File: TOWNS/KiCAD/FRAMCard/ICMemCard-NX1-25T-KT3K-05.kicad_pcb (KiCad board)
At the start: 2 copper layers, 79.1 x 50.5 mm, 19 parts, among them J1 PCMCIA_Connector, Q1 BC846X, Q2 BC846X, U1 FM18W08-SGTR, U2 FM18W08-SGTR, U3 74AHCT1G32

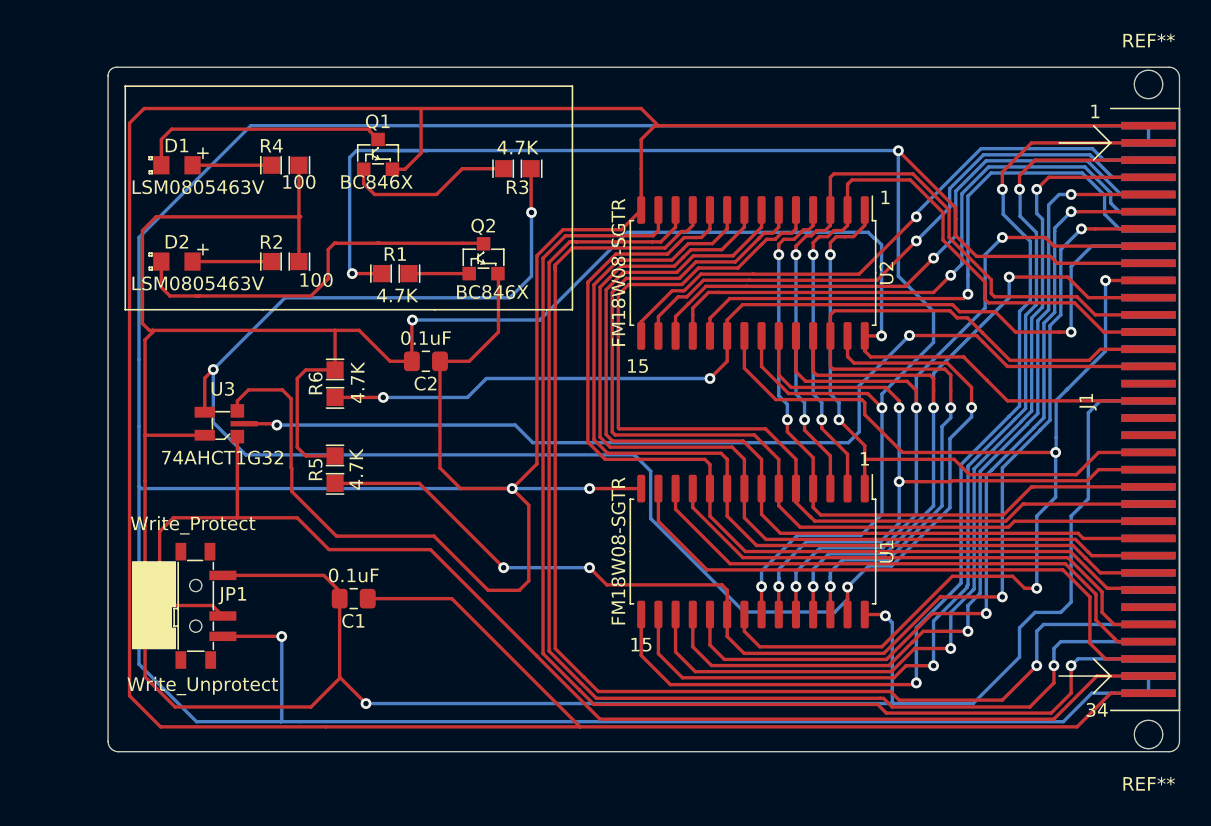
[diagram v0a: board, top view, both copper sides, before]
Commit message: Working on PCBfor Hirose NX1 PCMCIA Frame
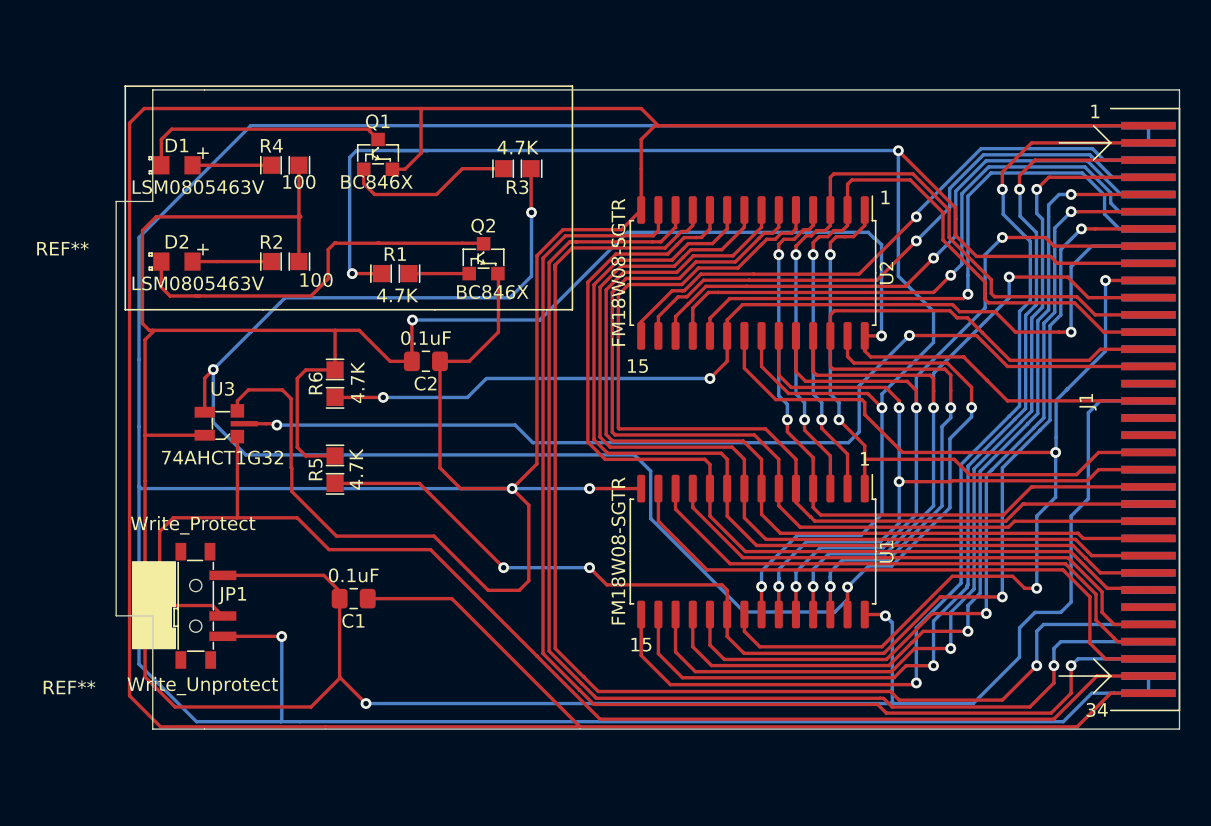
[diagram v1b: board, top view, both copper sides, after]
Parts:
- removed the REF** at (139.1, 99.9)
- removed the REF** at (139.1, 51.9)
- added REF**: MountingHole_1.5mm, MountingHole:MountingHole_2.1mm, F.Cu at (58.9, 60.4)
- added REF**: MountingHole_1.5mm, MountingHole:MountingHole_2.1mm, F.Cu at (59.3, 92.8)
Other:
- board size 79.1 x 50.5 mm -> 78.5 x 47.2 mm
- board text added: "FM TOWNS RESCUE BOOT MEMORY CARD Using HIROSE NX1 PCMCIA FRAME by Captain YS http://www.ysflight.com Ver. 20220514"
- board text added: "PCMCIA Connector"
- board text removed: "FM TOWNS RESCUE BOOT MEMORY CARD by Captain YS http://www.ysflight.com Ver. 20220514"
- board text removed: "PCMCIA Connector 95622-003LF"

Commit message: Added fillet
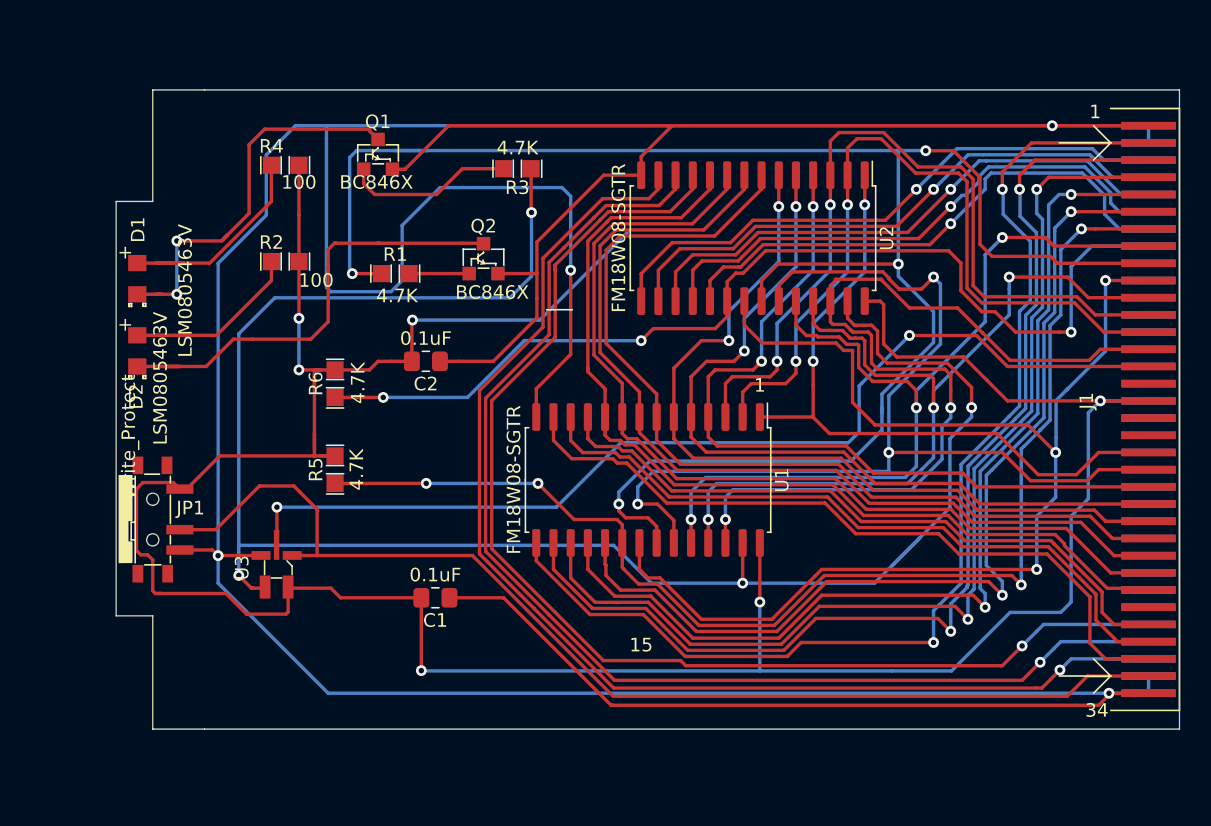
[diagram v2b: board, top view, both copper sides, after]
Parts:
- moved U3 11.3 mm to (74.7, 87.6), turned to 270 degrees
- moved REF** 9.67 mm to (68.5, 59.3)
- moved U1 9.38 mm to (102.1, 81.2)
- moved REF** 9.12 mm to (68.5, 92.5)
- moved D1 8.87 mm to (64.4, 66.3), turned to 90 degrees
- moved D2 7.22 mm to (64.4, 71.6), turned to 90 degrees
- moved JP1 7.12 mm to (65.5, 84.1)
- moved C1 6.03 mm to (86.4, 89.9)
- moved U2 2.57 mm to (109.9, 63.3)
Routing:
- net GND: track 555.9 -> 377.2 mm, vias 3 -> 4
- net Vcc: track 282.4 -> 212.6 mm, vias 4 -> 6
- net /A12: track 54.1 -> 75.6 mm
- net /Wp: track 96.8 -> 84.0 mm
- net /A6: track 70.7 -> 59.7 mm, vias 0 -> 2
- net Net-(D1-Pad1): track 18.6 -> 29.5 mm, vias 0 -> 2
- net Net-(D1-Pad2): track 5.83 -> 16.6 mm
- net /D0: track 39.5 -> 49.6 mm
- net /D1: track 41.6 -> 51.7 mm
- net /D7: track 62.5 -> 72.5 mm
- net /A11: track 82.5 -> 92.0 mm
- net /D2: track 44.8 -> 54.4 mm
- net /A5: track 70.6 -> 61.4 mm, vias 0 -> 2
- net /~OE: track 132.8 -> 141.9 mm
- net /D6: track 66.0 -> 74.7 mm
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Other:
- board text added: "Mounting Hole 2.1mm X 4.1mm Oval"
- board text removed: "Write_Unprotect"

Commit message: Cleaning up PCB
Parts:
- JP1: value Write_Protect -> WP
- U3: value 74AHCT1G32 -> SN74LS32DR; footprint PCMCIA:SOT353_Easy -> Package_SO:SOIC-14_3.9x8.7mm_P1.27mm
- moved U3 8.20 mm to (82.9, 88.1)
- moved C1 4.70 mm to (89.3, 93.5)
- moved R5 2.67 mm to (74.4, 80.4)
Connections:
- R1 pad 2: /~OE -> Net-(R1-Pad2)
- R3 pad 2: /~WE~orWP -> Net-(R3-Pad2)
- U3 pad 1: /Wp -> /WPorWP
- U3 pad 3: GND -> /~WE~orWP
- U3 pad 4: /~WE~orWP -> /Wp
- U3 pad 5: Vcc -> /Wp
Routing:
- net /~WE~orWP: track 136.5 -> 87.2 mm, vias 4 -> 3
- net /~OE: track 141.9 -> 103.5 mm, vias 4 -> 5
- net Net-(R3-Pad2): track 0.00 -> 38.3 mm, vias 0 -> 2
- net GND: track 377.2 -> 347.4 mm
- net Net-(R1-Pad2): track 0.00 -> 26.0 mm, vias 0 -> 2
- net /~WE: track 75.6 -> 64.3 mm
- net /WPorWP: track 0.00 -> 9.54 mm
- net /~CE1: track 91.8 -> 99.6 mm
- net Vcc: track 212.6 -> 204.8 mm
- net /Wp: track 84.0 -> 87.1 mm
- net /A14: track 68.0 -> 65.4 mm
- net /D11: track 43.7 -> 45.7 mm
- net /D7: track 72.5 -> 74.4 mm
- net /D12: track 42.7 -> 44.6 mm
- net /D6: track 74.7 -> 76.5 mm
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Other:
- outline, holes or cut-outs redrawn
- board text added: "FM TOWNS RESCUE BOOT MEMORY CARD Using HIROSE NX1 PCMCIA FRAME by Captain YS http://www.ysflight.com Ver. 20220520"
- board text removed: "FM TOWNS RESCUE BOOT MEMORY CARD Using HIROSE NX1 PCMCIA FRAME by Captain YS http://www.ysflight.com Ver. 20220514"

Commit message: Moving files around.
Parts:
- moved R5 32.8 mm to (106.2, 88.3), turned to 0 degrees
- moved R6 26.6 mm to (103.7, 73.3), turned to 180 degrees
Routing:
- net /~CE2: track 75.1 -> 48.3 mm, vias 3 -> 1
- net /~CE1: track 99.6 -> 75.2 mm
- net Vcc: track 204.8 -> 210.1 mm, vias 6 -> 7
- net /~OE: track 103.5 -> 104.6 mm
- net /A4: track 69.3 -> 70.0 mm
- net /A9: track 61.9 -> 62.4 mm

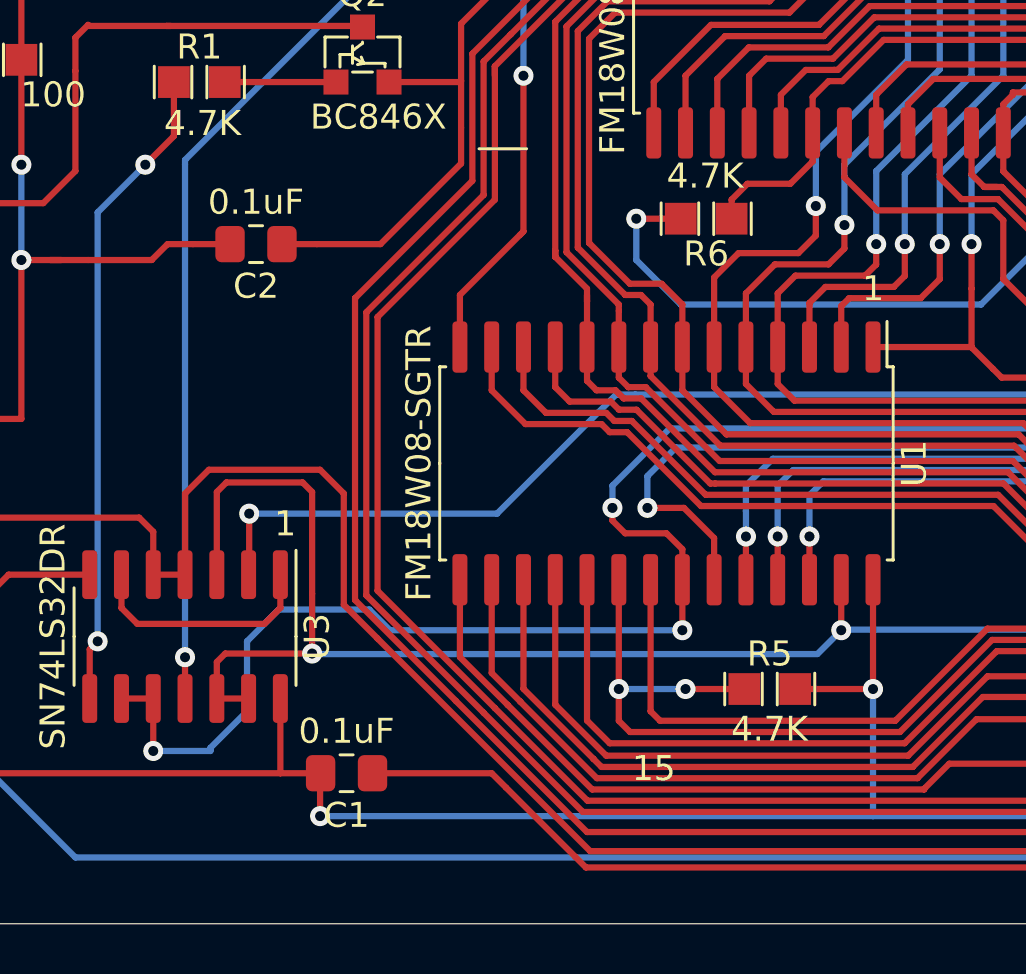
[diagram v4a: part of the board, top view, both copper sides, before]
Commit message: Better spacing between parts.
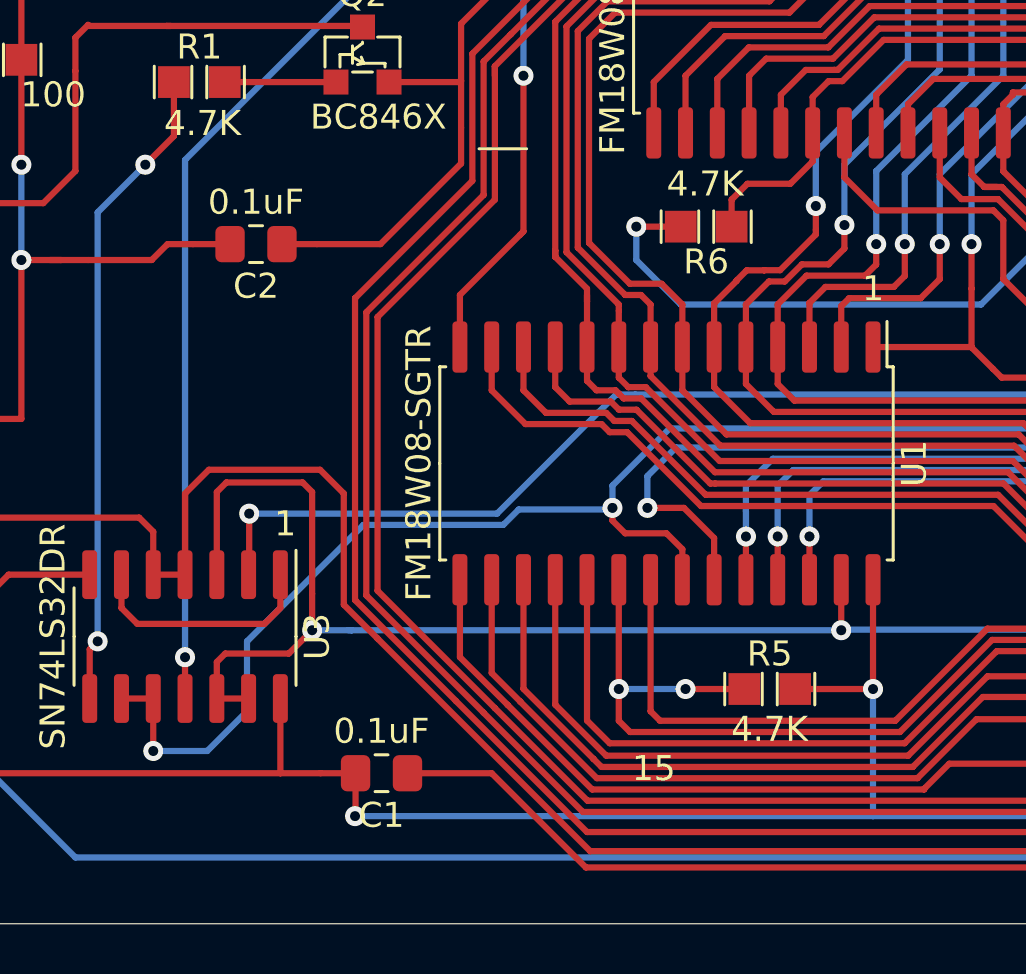
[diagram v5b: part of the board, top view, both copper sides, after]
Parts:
- moved C1 1.40 mm to (90.7, 93.5)
- moved R6 0.32 mm to (103.7, 73.6)
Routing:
- net /~OE: track 104.6 -> 101.0 mm, vias 5 -> 4
- net GND: track 347.4 -> 346.0 mm
- net /~WE~orWP: track 86.7 -> 85.9 mm
- net /A5: track 61.6 -> 61.0 mm

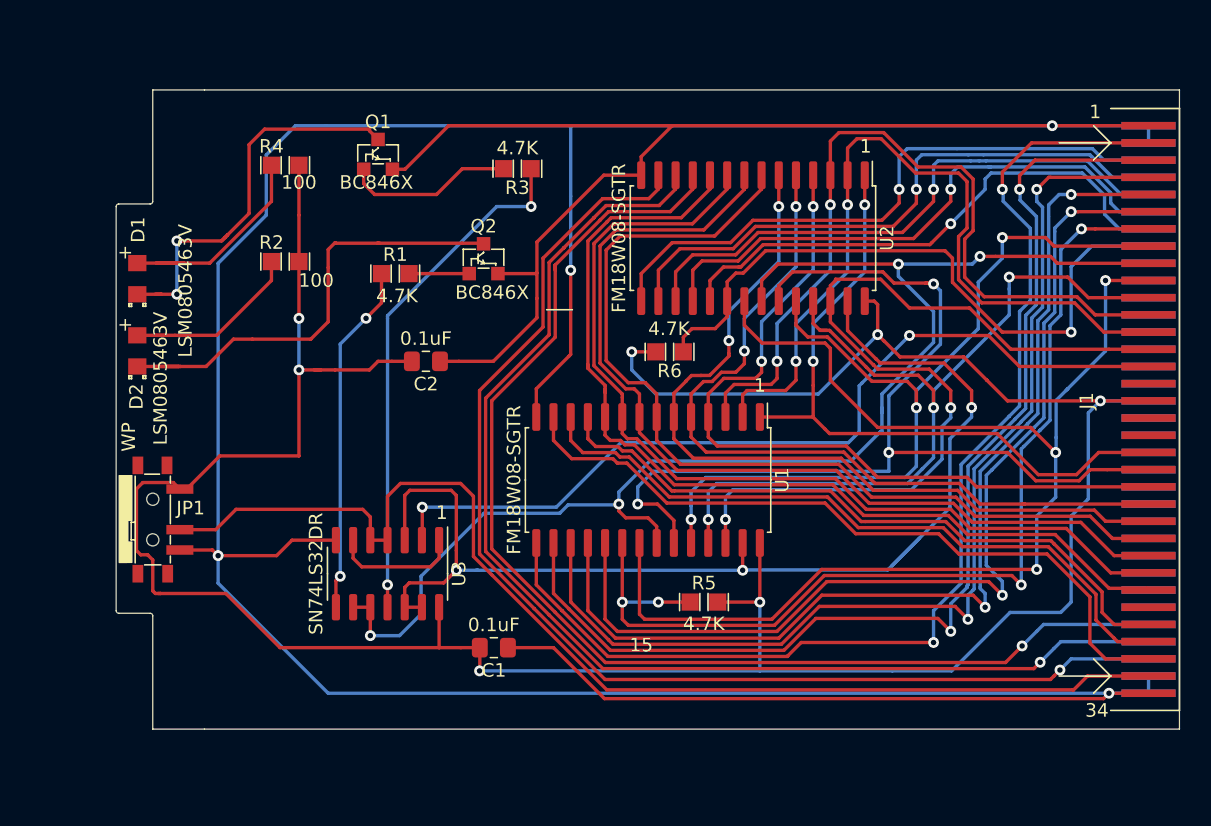
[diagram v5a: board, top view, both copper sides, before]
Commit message: Moving files around
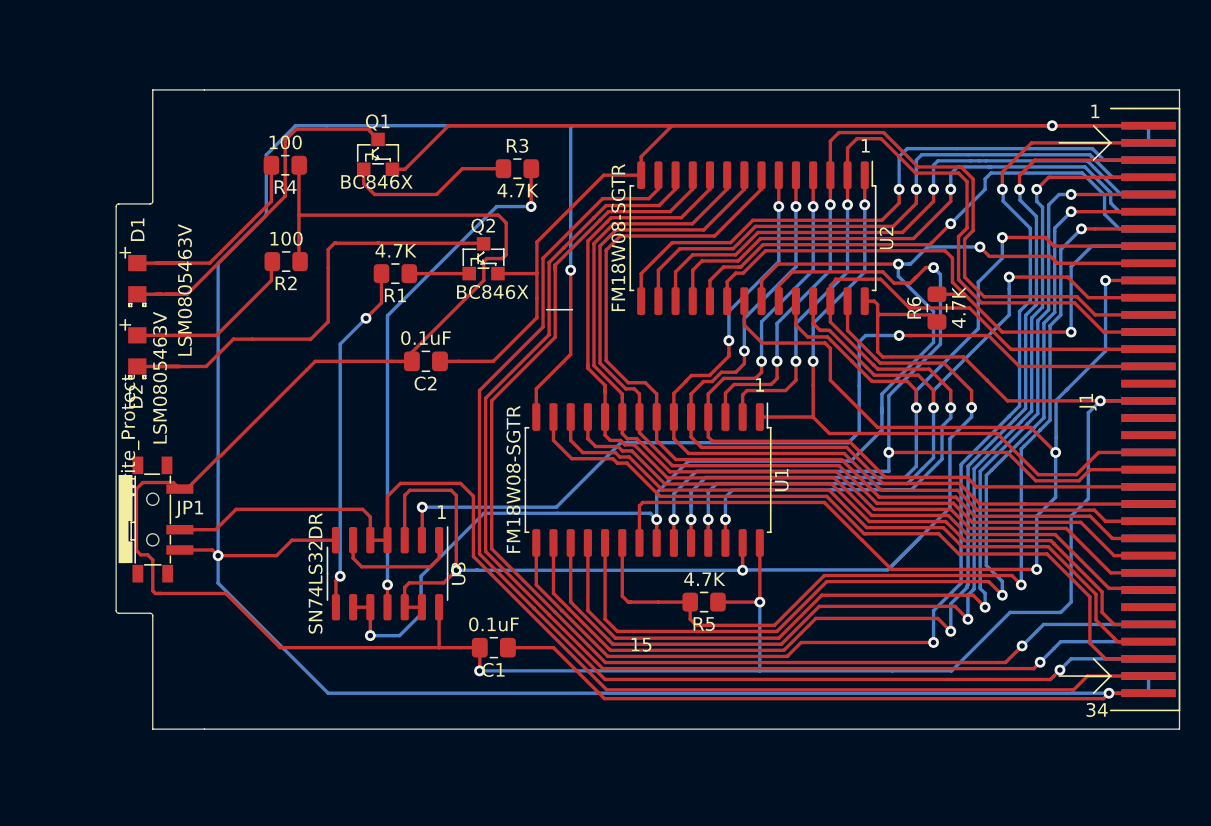
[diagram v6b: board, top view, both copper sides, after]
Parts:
- JP1: value WP -> Write_Protect
- R1, R2, R3, R4, R5, R6: footprint PCMCIA:KOA_RK73G2AAT -> Resistor_SMD:R_0805_2012Metric_Pad1.15x1.40mm_HandSolder
- moved R6 20.4 mm to (123.4, 68.5), turned to 90 degrees
- moved R2 1.91 mm to (75.4, 65.0), turned to 180 degrees
- moved R1 1.91 mm to (83.4, 65.9), turned to 180 degrees
- moved R4 1.91 mm to (75.3, 57.9), turned to 180 degrees
- moved R5 1.91 mm to (106.2, 90.2), turned to 180 degrees
- moved R3 1.91 mm to (92.5, 58.2), turned to 0 degrees
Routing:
- net /~CE1: track 75.2 -> 69.9 mm, vias 4 -> 2
- net /~CE2: track 48.6 -> 44.5 mm
- net /A12: track 74.6 -> 71.5 mm
- net Net-(D1-Pad1): track 29.5 -> 26.9 mm, vias 2 -> 0
- net /A11: track 93.1 -> 91.1 mm
- net /~WE: track 64.3 -> 66.3 mm
- net /~OE: track 101.0 -> 99.3 mm
- net Vcc: track 209.8 -> 208.6 mm, vias 7 -> 3

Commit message: Updated Schematic and PCB.
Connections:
- J1 pad 33: /Wp -> /WP
- JP1 pad 2: /Wp -> /WP
- R1 pad 2: Net-(R1-Pad2) -> /~OE
- R3 pad 2: Net-(R3-Pad2) -> /~WE~orWP
- U3 pad 1: /WPorWP -> /WP
- U3 pad 10: /~OE -> Net-(U3-Pad10)
- U3 pad 11: Net-(R3-Pad2) -> Net-(U3-Pad11)
- U3 pad 12: /~WE~orWP -> Net-(U3-Pad12)
- U3 pad 13: /~WE~orWP -> Net-(U3-Pad12)
- U3 pad 4: /Wp -> GND
- U3 pad 5: /Wp -> GND
- U3 pad 6: /WPorWP -> Net-(U3-Pad10)
- U3 pad 8: Net-(R1-Pad2) -> Net-(U3-Pad12)
- U3 pad 9: /~OE -> Net-(U3-Pad10)
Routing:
- net /WP: track 0.00 -> 93.5 mm
- net /Wp: track 87.1 -> 0.00 mm
- net /~WE~orWP: track 85.9 -> 134.3 mm, vias 3 -> 4
- net Net-(R3-Pad2): track 38.3 -> 0.00 mm, vias 2 -> 0
- net Net-(R1-Pad2): track 26.0 -> 0.00 mm, vias 2 -> 0
- net /~OE: track 99.3 -> 110.0 mm
- net Net-(U3-Pad12): track 0.00 -> 9.91 mm
- net /WPorWP: track 9.54 -> 0.00 mm
- net GND: track 346.0 -> 353.1 mm
- net Net-(U3-Pad10): track 0.00 -> 6.22 mm
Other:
- board text added: "FM TOWNS RESCUE BOOT MEMORY CARD Using HIROSE NX1 PCMCIA FRAME by Captain YS http://www.ysflight.com Ver. 20220525"
- board text removed: "FM TOWNS RESCUE BOOT MEMORY CARD Using HIROSE NX1 PCMCIA FRAME by Captain YS http://www.ysflight.com Ver. 20220520"
